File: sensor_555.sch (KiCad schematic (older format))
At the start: 6 parts, among them J1 Conn_01x03_Male, U1 SA555

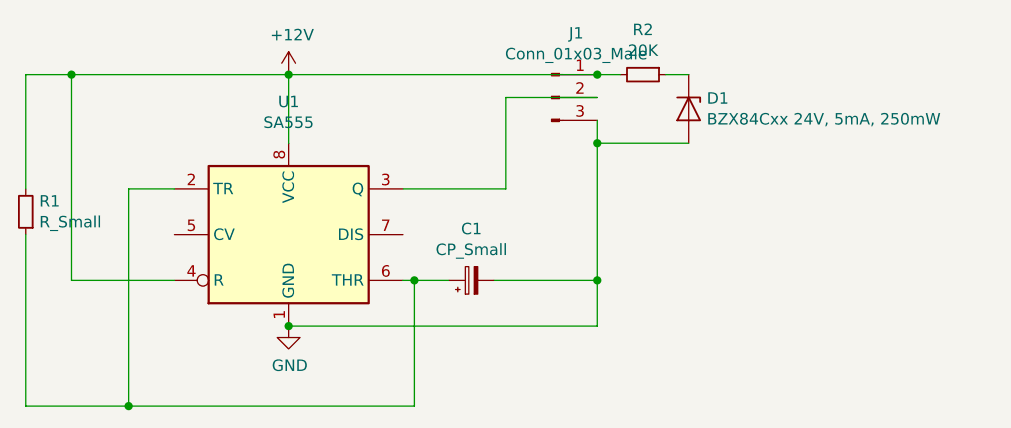
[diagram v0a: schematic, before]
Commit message: [FEAT]: sch is updated (values noted)
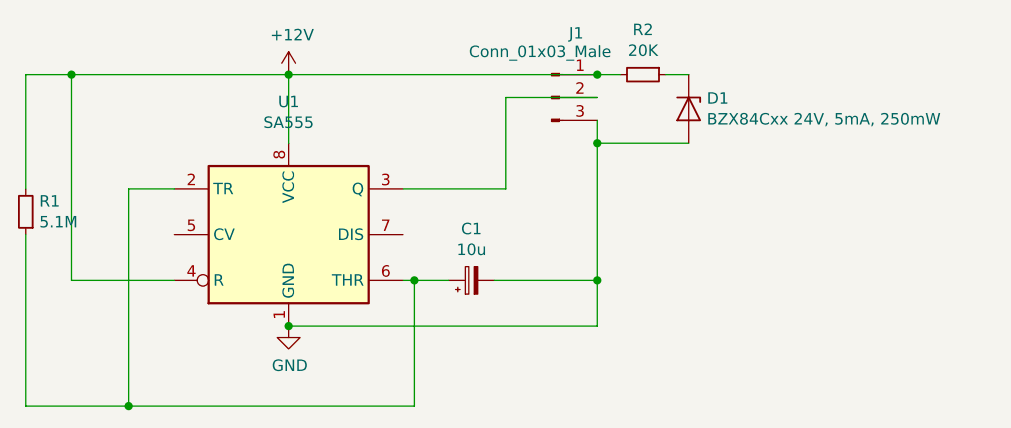
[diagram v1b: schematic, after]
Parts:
- C1: value CP_Small -> 10u; Voltage (none) -> 35
- R1: value R_Small -> 5.1M
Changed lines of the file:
@@
 EESchema Schematic File Version 4
+LIBS:sensor_555-cache
 EELAYER 30 0
 EELAYER END
@@
 P 6300 3900
 F 0 "C1" V 6525 3900 50  0000 C CNN
-F 1 "CP_Small" V 6434 3900 50  0000 C CNN
+F 1 "10u" V 6434 3900 50  0000 C CNN
 F 2 "Capacitor_Tantalum_SMD:CP_EIA-7343-31_Kemet-D" H 6300 3900 50  0001 C CNN
 F 3 "~" H 6300 3900 50  0001 C CNN
+F 4 "35" V 6300 3900 50  0001 C CNN "Voltage"
 	1    6300 3900
 	0    -1   -1   0
@@
 P 4350 3600
 F 0 "R1" H 4291 3554 50  0000 R CNN
-F 1 "R_Small" H 4291 3645 50  0000 R CNN
+F 1 "5.1M" H 4291 3645 50  0000 R CNN
 F 2 "Resistor_SMD:R_1206_3216Metric_Pad1.42x1.75mm_HandSolder" H 4350 3600 50  0001 C CNN
 F 3 "~" H 4350 3600 50  0001 C CNN
@@
 P 6650 3100
 F 0 "J1" H 6758 3381 50  0000 C CNN
-F 1 "Conn_01x03_Male" H 6758 3290 50  0000 C CNN
+F 1 "Conn_01x03_Male" H 6600 3300 50  0000 C CNN
 F 2 "Connector_PinHeader_2.54mm:PinHeader_1x03_P2.54mm_Horizontal" H 6650 3100 50  0001 C CNN
 F 3 "~" H 6650 3100 50  0001 C CNN
